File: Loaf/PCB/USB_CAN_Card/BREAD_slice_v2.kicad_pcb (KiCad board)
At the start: 2 copper layers, 100 x 70.6 mm, 23 parts, among them J1 10018783-10200TLF, P2 USB_B, U1 MCP2210x-SO, U2 MCP2515-xSO, U3 MCP2561-E-P, Y1 12MHZ Crystal, Y2 16MHZ Crystal

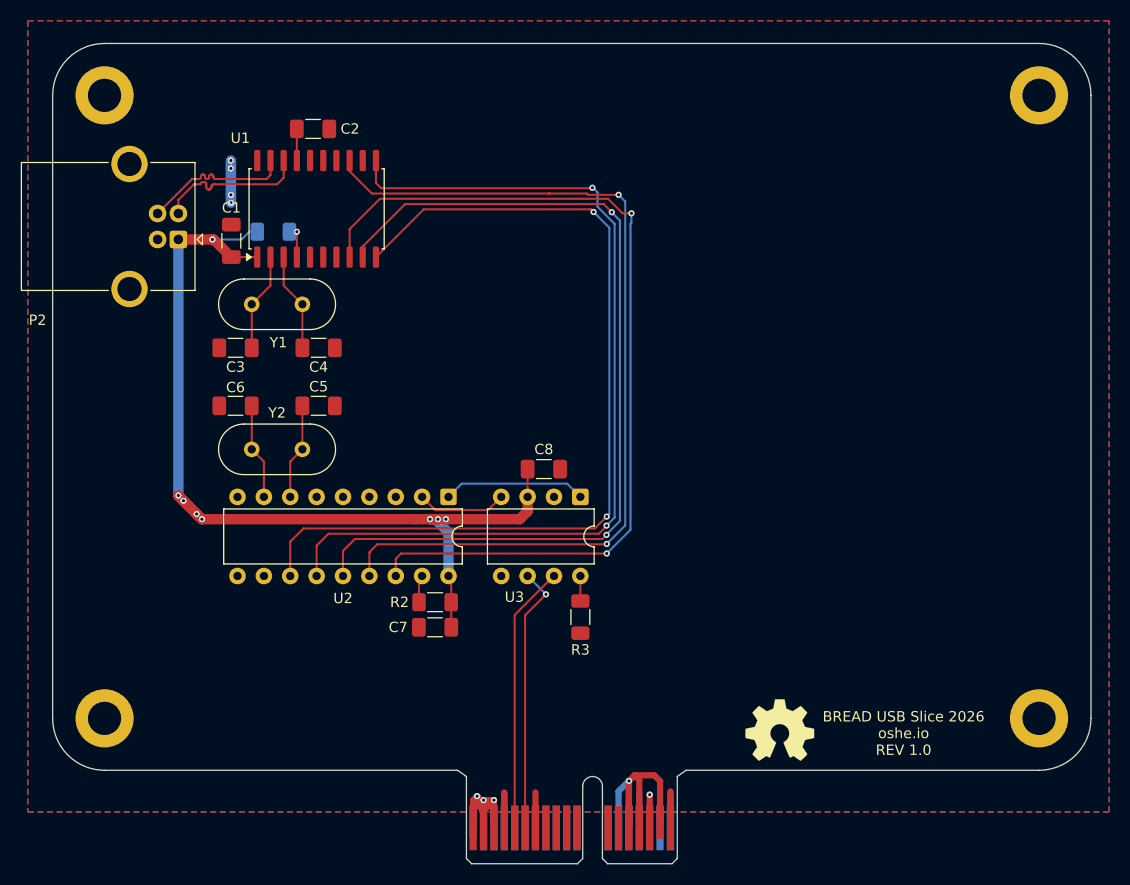
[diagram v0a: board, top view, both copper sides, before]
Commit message: Updated DRC to fit new OSHE specs
pain
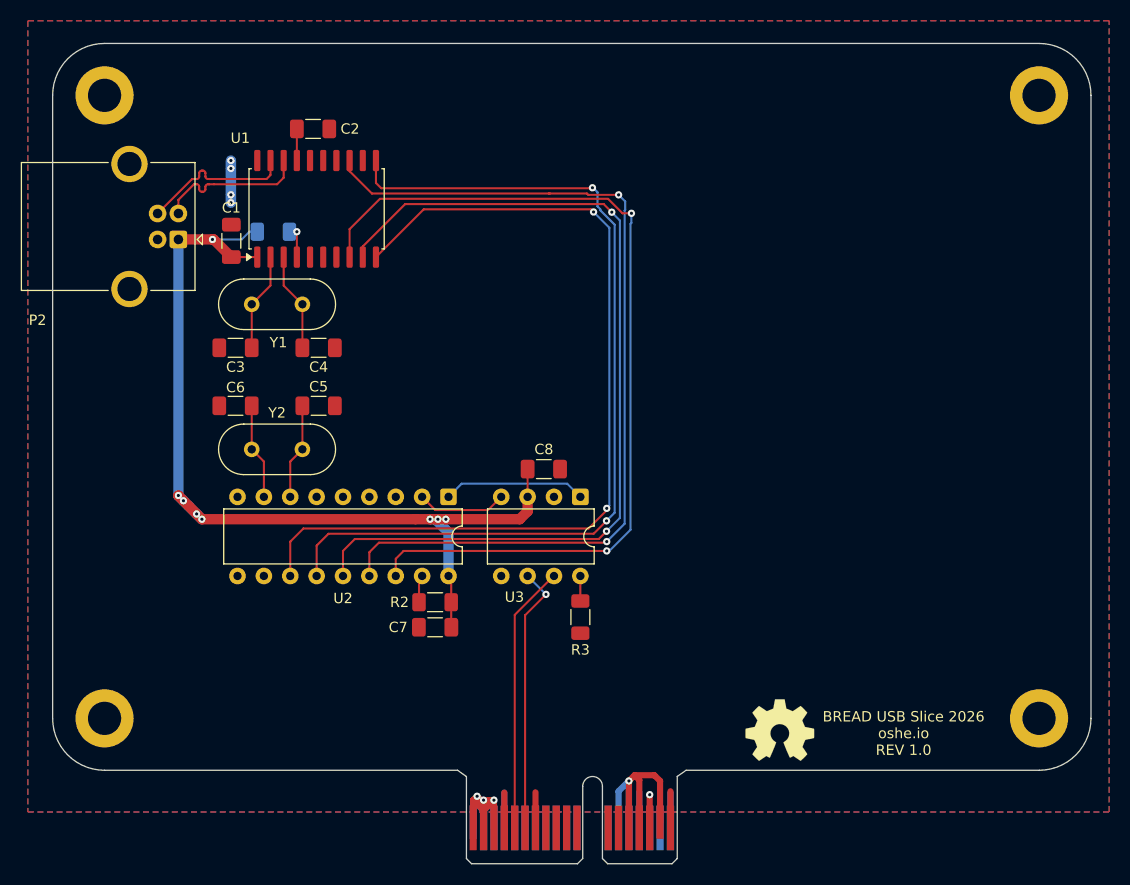
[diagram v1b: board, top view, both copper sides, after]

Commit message: Added OSHE branding to VRM
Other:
- board text added: "BREAD USB Slice 2026 oshe.io Rev 1.0"
- board text removed: "BREAD USB Slice 2026 oshe.io REV 1.0"
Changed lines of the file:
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@@
 		(layer "Edge.Cuts")
 	)
-	(gr_text "BREAD USB Slice 2026\noshe.io\nREV 1.0"
+	(gr_text "BREAD USB Slice 2026\noshe.io\nRev 1.0"
 		(at 183.404 124.166 0)
 		(layer "F.SilkS")

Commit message: Slight updates
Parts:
- C1: value 2uF -> 1uF
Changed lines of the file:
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@@
 			)
 		)
-		(property "Value" "2uF"
+		(property "Value" "1uF"
 			(at -1.0047 -7.453 180)
 			(layer "F.Fab")

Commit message: Peter recommended PCB changes
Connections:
- J1 pad A1: +12V -> Net-(J1-PadA1)
- J1 pad A2: +12V -> Net-(J1-PadA1)
- J1 pad A3: +12V -> Net-(J1-PadA1)
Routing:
- net +12V: track 29.9 -> 14.5 mm, vias 3 -> 0
- net Net-(J1-PadA1): track 0.00 -> 14.5 mm
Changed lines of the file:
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@@
 			(size 0.7 3.2)
 			(layers "B.Cu" "B.Mask")
-			(net "+12V")
+			(net "Net-(J1-PadA1)")
 			(pinfunction "A1_A1")
 			(pintype "passive")
@@
 			(size 0.7 4.3)
 			(layers "B.Cu" "B.Mask")
-			(net "+12V")
+			(net "Net-(J1-PadA1)")
 			(pinfunction "A2_A2")
 			(pintype "passive")
@@
 			(size 0.7 4.3)
 			(layers "B.Cu" "B.Mask")
-			(net "+12V")
+			(net "Net-(J1-PadA1)")
 			(pinfunction "A3_A3")
 			(pintype "passive")
@@
 	)
 	(segment
+		(start 142.699478 128.400522)
+		(end 142.7 128.4)
+		(width 0.6)
+		(layer "F.Cu")
+		(net "+12V")
+	)
+	(segment
 		(start 143.949478 131.074)
 		(end 143.949478 128.400522)
@@
 	)
 	(segment
-		(start 142.95 128.4)
-		(end 142.7 128.4)
+		(start 141.949478 128.400522)
+		(end 142.699478 128.400522)
 		(width 0.6)
 		(layer "F.Cu")
@@
 	)
 	(segment
-		(start 141.949478 128.400522)
-		(end 142.325 128.025)
-		(width 0.6)
-		(layer "F.Cu")
-		(net "+12V")
-	)
-	(segment
 		(start 142.949478 131.074)
 		(end 142.949478 129.400522)
@@
 	)
 	(segment
-		(start 142.949478 128.400522)
+		(start 142.7 128.4)
 		(end 142.95 128.4)
 		(width 0.6)
@@
 	)
 	(segment
-		(start 142.7 128.4)
-		(end 142.325 128.025)
+		(start 142.949478 128.400522)
+		(end 142.95 128.4)
 		(width 0.6)
 		(layer "F.Cu")
@@
 		(net "+12V")
 	)
-	(via
-		(at 142.95 128.4)
-		(size 0.7064)
-		(drill 0.3)
-		(layers "F.Cu" "B.Cu")
-		(net "+12V")
-	)
-	(via
-		(at 143.95 128.4)
-		(size 0.7064)
-		(drill 0.3)
-		(layers "F.Cu" "B.Cu")
-		(net "+12V")
-	)
-	(via
-		(at 142.325 128.025)
-		(size 0.7064)
-		(drill 0.3)
-		(layers "F.Cu" "B.Cu")
-		(net "+12V")
-	)
-	(segment
-		(start 141.95 128.4)
-		(end 142.325 128.025)
-		(width 0.6)
-		(layer "B.Cu")
-		(net "+12V")
-	)
-	(segment
-		(start 142.95 129.4)
-		(end 143.95 128.4)
-		(width 0.6)
-		(layer "B.Cu")
-		(net "+12V")
-	)
-	(segment
-		(start 141.95 131.073478)
-		(end 141.95 128.4)
-		(width 0.6)
-		(layer "B.Cu")
-		(net "+12V")
-	)
-	(segment
-		(start 143.95 131.073478)
-		(end 143.95 128.4)
-		(width 0.6)
-		(layer "B.Cu")
-		(net "+12V")
-	)
-	(segment
-		(start 142.95 131.073478)
-		(end 142.95 128.4)
-		(width 0.6)
-		(layer "B.Cu")
-		(net "+12V")
-	)
-	(segment
-		(start 142.325 128.025)
-		(end 142.699478 128.399478)
-		(width 0.6)
-		(layer "B.Cu")
-		(net "+12V")
-	)
-	(segment
-		(start 142.95 128.4)
-		(end 142.949478 128.399478)
-		(width 0.6)
-		(layer "B.Cu")
-		(net "+12V")
-	)
-	(segment
-		(start 143.95 128.4)
-		(end 143.949478 128.399478)
-		(width 0.6)
-		(layer "B.Cu")
-		(net "+12V")
-	)
-	(segment
-		(start 142.699478 128.399478)
-		(end 142.949478 128.399478)
-		(width 0.6)
-		(layer "B.Cu")
-		(net "+12V")
-	)
-	(segment
-		(start 142.325 128.775)
-		(end 142.325 128.025)
-		(width 0.6)
-		(layer "B.Cu")
-		(net "+12V")
-	)
-	(segment
-		(start 142.95 131.073478)
-		(end 142.95 129.4)
-		(width 0.6)
-		(layer "B.Cu")
-		(net "+12V")
-	)
-	(segment
-		(start 142.949478 128.399478)
-		(end 143.949478 128.399478)
-		(width 0.6)
-		(layer "B.Cu")
-		(net "+12V")
-	)
-	(segment
-		(start 142.95 129.4)
-		(end 142.325 128.775)
-		(width 0.6)
-		(layer "B.Cu")
-		(net "+12V")
-	)
 	(segment
 		(start 156.949478 126.550522)
@@
 		(net "MISO")
 	)
+	(segment
+		(start 142.95 129.4)
+		(end 143.95 128.4)
+		(width 0.6)
+		(layer "B.Cu")
+		(net "Net-(J1-PadA1)")
+	)
+	(segment
+		(start 141.95 128.401044)
+		(end 141.95 131.073478)
+		(width 0.6)
+		(layer "B.Cu")
+		(net "Net-(J1-PadA1)")
+	)
+	(segment
+		(start 143.95 131.073478)
+		(end 143.95 128.4)
+		(width 0.6)
+		(layer "B.Cu")
+		(net "Net-(J1-PadA1)")
+	)
+	(segment
+		(start 142.95 131.073478)
+		(end 142.95 128.4)
+		(width 0.6)
+		(layer "B.Cu")
+		(net "Net-(J1-PadA1)")
+	)
+	(segment
+		(start 141.949478 128.400522)
+		(end 142.698434 128.400522)
+		(width 0.6)
+		(layer "B.Cu")
+		(net "Net-(J1-PadA1)")
+	)
+	(segment
+		(start 142.699478 128.399478)
+		(end 142.949478 128.399478)
+		(width 0.6)
+		(layer "B.Cu")
+		(net "Net-(J1-PadA1)")
+	)
+	(segment
+		(start 142.698434 128.400522)
+		(end 142.699478 128.399478)
+		(width 0.6)
+		(layer "B.Cu")
+		(net "Net-(J1-PadA1)")
+	)
+	(segment
+		(start 141.949478 128.400522)
+		(end 141.95 128.401044)
+		(width 0.6)
+		(layer "B.Cu")
+		(net "Net-(J1-PadA1)")
+	)
+	(segment
+		(start 142.323956 128.775)
+		(end 142.325 128.775)
+		(width 0.6)
+		(layer "B.Cu")
+		(net "Net-(J1-PadA1)")
+	)
+	(segment
+		(start 142.95 128.4)
+		(end 142.949478 128.399478)
+		(width 0.6)
+		(layer "B.Cu")
+		(net "Net-(J1-PadA1)")
+	)
+	(segment
+		(start 143.95 128.4)
+		(end 143.949478 128.399478)
+		(width 0.6)
+		(layer "B.Cu")
+		(net "Net-(J1-PadA1)")
+	)
+	(segment
+		(start 142.95 131.073478)
+		(end 142.95 129.4)
+		(width 0.6)
+		(layer "B.Cu")
+		(net "Net-(J1-PadA1)")
+	)
+	(segment
+		(start 142.949478 128.399478)
+		(end 143.949478 128.399478)
+		(width 0.6)
+		(layer "B.Cu")
+		(net "Net-(J1-PadA1)")
+	)
+	(segment
+		(start 141.949478 128.400522)
+		(end 142.323956 128.775)
+		(width 0.6)
+		(layer "B.Cu")
+		(net "Net-(J1-PadA1)")
+	)
+	(segment
+		(start 142.325 128.775)
+		(end 142.95 129.4)
+		(width 0.6)
+		(layer "B.Cu")
+		(net "Net-(J1-PadA1)")
+	)
 	(zone
